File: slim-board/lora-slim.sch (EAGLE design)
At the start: 26 parts, among them IC1 STM32F030F4, IC2 ADP1607, J1 SWD_PTH_SHROUD, X1 SMA-142-0701-801/806, X2 UBLOX_MAX, X3 RFM98

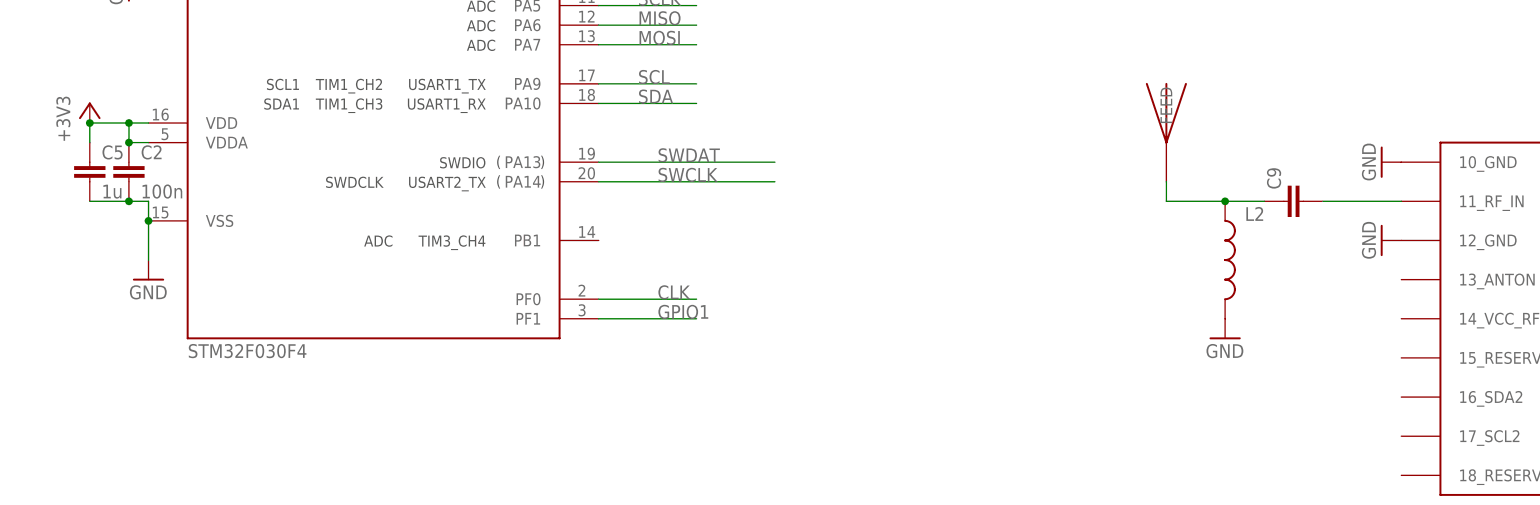
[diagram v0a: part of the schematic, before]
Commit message: Update slim-lora board. [inverted battery, remove gps rf parts, rework reg layout, add gpio1 header]
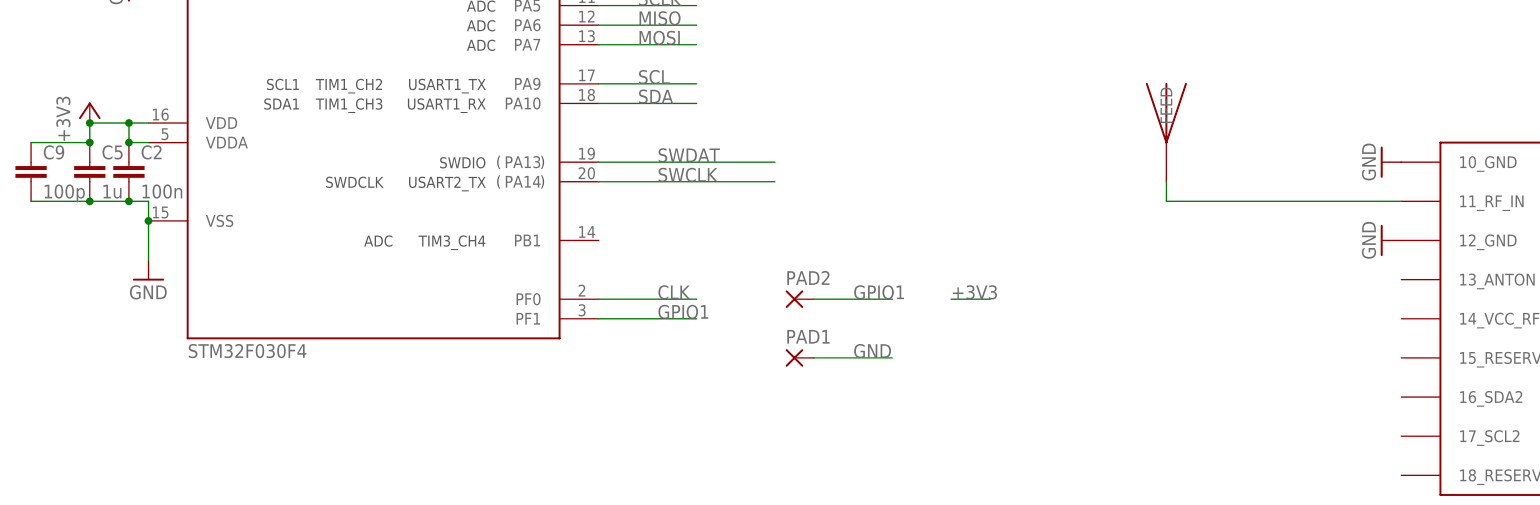
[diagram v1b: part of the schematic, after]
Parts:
- removed L2: (no value), SparkFun-Passives:INDUCTOR0603
- added PAD1, PAD2: (no value), wirepad:2,15/1,0
- C9: value (none) -> 100p
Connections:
- removed net N$4: C9.1, L2.1, U$5.FEED
- net +3V3: now also C9.1
- net GND: now also C9.2, PAD1.P; no longer L2.2
- net GPIO1: now also PAD2.P
- net N$1: now also U$5.FEED; no longer C9.2
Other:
- moved on the sheet: C9
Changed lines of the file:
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@@
 <?xml version="1.0" encoding="utf-8"?>
 <!DOCTYPE eagle SYSTEM "eagle.dtd">
-<eagle version="6.5.0">
+<eagle version="6.6.0">
 <drawing>
 <settings>
@@
 <part name="R5" library="rcl" deviceset="R-EU_" device="R0603" value="10k"/>
 <part name="+3V8" library="supply1" deviceset="+3V3" device=""/>
-<part name="C9" library="rcl" deviceset="C-EU" device="C0603"/>
-<part name="L2" library="SparkFun-Passives" deviceset="INDUCTOR" device="0603"/>
-<part name="GND19" library="supply1" deviceset="GND" device=""/>
 <part name="TP2" library="testpad" deviceset="PTR1" device="B1,27"/>
 <part name="TP3" library="testpad" deviceset="PTR1" device="B1,27"/>
@@
 <part name="GND23" library="supply1" deviceset="GND" device=""/>
 <part name="L3" library="SparkFun-Passives" deviceset="INDUCTOR" device="1210"/>
+<part name="C9" library="rcl" deviceset="C-EU" device="C0603" value="100p"/>
+<part name="PAD1" library="wirepad" deviceset="2,15/1,0" device=""/>
+<part name="PAD2" library="wirepad" deviceset="2,15/1,0" device=""/>
 </parts>
 <sheets>
@@
 <instance part="R5" gate="G$1" x="96.52" y="27.94" rot="R180"/>
 <instance part="+3V8" gate="G$1" x="7.62" y="5.08"/>
-<instance part="C9" gate="G$1" x="162.56" y="-7.62" rot="R90"/>
-<instance part="L2" gate="G$1" x="154.94" y="-15.24"/>
-<instance part="GND19" gate="1" x="154.94" y="-25.4"/>
 <instance part="TP2" gate="G$1" x="241.3" y="-38.1" rot="R90"/>
 <instance part="TP3" gate="G$1" x="241.3" y="-33.02" rot="R90"/>
@@
 <instance part="GND23" gate="1" x="101.6" y="124.46" rot="R270"/>
 <instance part="L3" gate="G$1" x="149.86" y="88.9" rot="R90"/>
+<instance part="C9" gate="G$1" x="0" y="-2.54"/>
+<instance part="PAD1" gate="1" x="99.06" y="-27.94"/>
+<instance part="PAD2" gate="1" x="99.06" y="-20.32"/>
 </instances>
 <busses>
@@
 <pinref part="C2" gate="G$1" pin="2"/>
 <junction x="12.7" y="-7.62"/>
+<pinref part="C9" gate="G$1" pin="2"/>
+<wire x1="0" y1="-7.62" x2="7.62" y2="-7.62" width="0.1524" layer="91"/>
+<junction x="7.62" y="-7.62"/>
 </segment>
 <segment>
@@
 </segment>
 <segment>
-<pinref part="L2" gate="G$1" pin="2"/>
-<pinref part="GND19" gate="1" pin="GND"/>
-</segment>
-<segment>
 <pinref part="TP1" gate="G$1" pin="TP"/>
 <pinref part="GND20" gate="1" pin="GND"/>
@@
 <pinref part="X1" gate="G1" pin="2"/>
 <pinref part="GND23" gate="1" pin="GND"/>
+</segment>
+<segment>
+<wire x1="111.76" y1="-27.94" x2="101.6" y2="-27.94" width="0.1524" layer="91"/>
+<label x="106.68" y="-27.94" size="1.778" layer="95"/>
+<pinref part="PAD1" gate="1" pin="P"/>
 </segment>
 </net>
@@
 <pinref part="+3V8" gate="G$1" pin="+3V3"/>
 <junction x="7.62" y="2.54"/>
+<pinref part="C9" gate="G$1" pin="1"/>
+<wire x1="0" y1="0" x2="7.62" y2="0" width="0.1524" layer="91"/>
+<junction x="7.62" y="0"/>
+</segment>
+<segment>
+<wire x1="119.38" y1="-20.32" x2="124.46" y2="-20.32" width="0.1524" layer="91"/>
+<label x="119.38" y="-20.32" size="1.778" layer="95"/>
 </segment>
 </net>
@@
 <pinref part="IC1" gate="G$1" pin="PF1"/>
 <wire x1="73.66" y1="-22.86" x2="86.36" y2="-22.86" width="0.1524" layer="91"/>
+</segment>
+<segment>
+<wire x1="101.6" y1="-20.32" x2="111.76" y2="-20.32" width="0.1524" layer="91"/>
+<label x="106.68" y="-20.32" size="1.778" layer="95"/>
+<pinref part="PAD2" gate="1" pin="P"/>
 </segment>
 </net>
@@
 <segment>
 <pinref part="X2" gate="G$1" pin="11_RF_IN"/>
-<pinref part="C9" gate="G$1" pin="2"/>
-<wire x1="177.8" y1="-7.62" x2="167.64" y2="-7.62" width="0.1524" layer="91"/>
-</segment>
-</net>
-<net name="N$4" class="0">
-<segment>
-<pinref part="C9" gate="G$1" pin="1"/>
 <pinref part="U$5" gate="G$1" pin="FEED"/>
-<wire x1="160.02" y1="-7.62" x2="154.94" y2="-7.62" width="0.1524" layer="91"/>
-<wire x1="154.94" y1="-7.62" x2="147.32" y2="-7.62" width="0.1524" layer="91"/>
+<wire x1="177.8" y1="-7.62" x2="147.32" y2="-7.62" width="0.1524" layer="91"/>
 <wire x1="147.32" y1="-7.62" x2="147.32" y2="-5.08" width="0.1524" layer="91"/>
-<pinref part="L2" gate="G$1" pin="1"/>
-<junction x="154.94" y="-7.62"/>
-</segment>
-</net>
+</segment>
+</net>

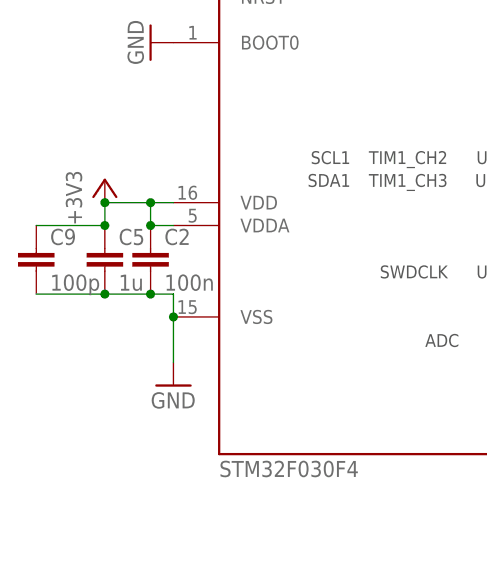
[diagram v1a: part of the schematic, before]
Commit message: slim-board: Tweak cap values.
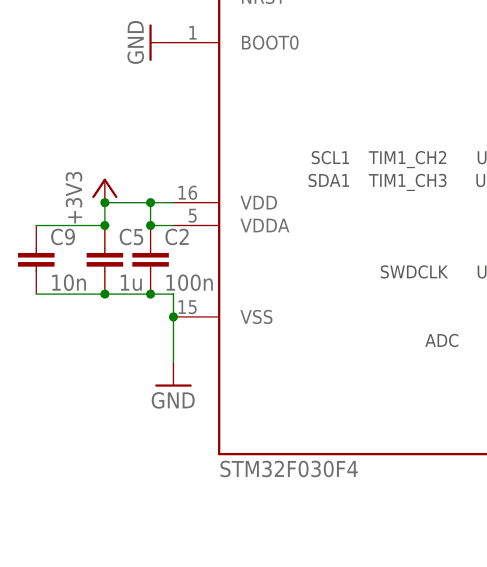
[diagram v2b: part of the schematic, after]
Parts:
- C9: value 100p -> 10n
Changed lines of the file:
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@@
 <part name="GND23" library="supply1" deviceset="GND" device=""/>
 <part name="L3" library="SparkFun-Passives" deviceset="INDUCTOR" device="1210"/>
-<part name="C9" library="rcl" deviceset="C-EU" device="C0603" value="100p"/>
+<part name="C9" library="rcl" deviceset="C-EU" device="C0603" value="10n"/>
 <part name="PAD1" library="wirepad" deviceset="2,15/1,0" device=""/>
 <part name="PAD2" library="wirepad" deviceset="2,15/1,0" device=""/>
